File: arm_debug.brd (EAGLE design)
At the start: 40.3 x 19 mm, 11 parts

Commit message: Saving place.. currently working on Rev B
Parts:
- removed DEBUG: (no value), pinhead:1X06
- removed LED2: (no value), led:SML0805
- removed TP_5V, TP_GND0, TP_GND1, TP_VCC: 1625854-3, 1625854-3:RESC1608X50N
- added C1, C2: (no value), resistor:C0805
- added IC1: FT230XSS, FT230XS:SSOP16
- added JP1, JP2, PWR_SELECT: (no value), pinhead:1X03
- added P1: 0473460001, 0473460001:MOLEX_0473460001
- added R2, R3, R4, R6, R7: (no value), resistor:R0805
- added TP1, TP2, TP4: TPTP20SQ, testpad:TP20SQ
- added U1: CAT6219, CAT6219-330TDGT3:SOT-23(OT)5_LEAD
- moved LED1 16.1 mm to (29.2, 23.5), turned to 270 degrees
- moved R1 13.5 mm to (40.6, 17.1)
- moved DEVICE 8.98 mm to (21.6, 21.6)
- moved PROG 8.98 mm to (8.89, 21.6)
- moved R5 6.84 mm to (29.2, 19.1)
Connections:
- removed net !CTS: DEBUG.2
- removed net !RTS: DEBUG.6
- removed net VCC: DEVICE.1, PROG.1, R1.2, TP_VCC.1, TP_VCC.2
- new net +3V3: PWR_SELECT.3, TP2.TP, U1.5
- new net D+: C2.1, IC1.8, R7.1
- new net D-: C1.1, IC1.9, R1.1
- new net FT230_RX: IC1.4, JP1.2
- new net FT230_TX: IC1.1, JP2.2
- new net N$3: IC1.10, IC1.11, IC1.3
- new net N$4: P1.3, R7.2
- new net N$7: JP2.3, R4.1, R6.2
- new net N$8: JP1.3, R2.2, R3.1
- new net TARGET_PWR: DEVICE.1, PROG.1, PWR_SELECT.2
- net +5V: now also IC1.12, P1.1, PWR_SELECT.1, TP1.TP, U1.1, U1.3; no longer DEBUG.3, TP_5V.1, TP_5V.2
- net DEBUG_UART_RX: now also JP2.1, R4.2; no longer DEBUG.4
- net DEBUG_UART_TX: now also JP1.1, R3.2; no longer DEBUG.5
- net GND: now also C1.2, C2.2, IC1.13, IC1.5, P1.5, R2.1, R6.1, TP4.TP, U1.2; no longer DEBUG.1, LED2.C, TP_GND0.1, TP_GND0.2, TP_GND1.1, TP_GND1.2
- net N$2: now also P1.2, R1.2; no longer LED2.A, R1.1
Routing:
- net TARGET_PWR: track 0.00 -> 76.4 mm, vias 0 -> 2
- net +5V: track 43.8 -> 97.9 mm, vias 0 -> 3
- net +3V3: track 0.00 -> 44.3 mm
- net VCC: track 43.0 -> 0.00 mm
- net D+: track 0.00 -> 21.3 mm
- net FT230_TX: track 0.00 -> 20.5 mm
- net DEBUG_UART_TX: track 19.5 -> 38.9 mm, vias 2 -> 1
- net D-: track 0.00 -> 15.7 mm
- net FT230_RX: track 0.00 -> 12.3 mm
- net GND: track 32.0 -> 41.4 mm, vias 5 -> 1
- net N$3: track 0.00 -> 7.14 mm
- net N$8: track 0.00 -> 6.75 mm
- net N$7: track 0.00 -> 6.75 mm
- net N$4: track 0.00 -> 4.98 mm
- net DEBUG_UART_RX: track 27.6 -> 31.6 mm, vias 2 -> 1
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- added copper zone on layer 1, net GND
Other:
- board size 40.3 x 19 mm -> 50.5 x 27.9 mm
- board text added: "+3.3V"
- board text added: "+5V"
- board text added: "GND"
- board text added: "Power Select"
- board text added: "Rev B"
- board text added: "TARGET"
- board text added: "UART Level Shift"
- board text removed: "Rev A"

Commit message: Committing RevB
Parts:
- removed IC1: FT230XSS, FT230XS:SSOP16
- removed JP1, JP2, PWR_SELECT: (no value), pinhead:1X03
- removed R6: (no value), resistor:R0805
- removed TP1, TP2, TP4: TPTP20SQ, testpad:TP20SQ
- added C3: .1uF, resistor:C0603
- added LED2, LED3: (no value), led:CHIPLED_0603
- added S1: 431151015826, 431151015826:431181015816
- C1, C2: value (none) -> 47pF; device resistor:C0805 -> resistor:C0603
- LED1: device led:SML0805 -> led:CHIPLED_0603
- R1, R4, R7: value (none) -> 27; device resistor:R0805 -> resistor:R0603
- R2, R3: value (none) -> 330; device resistor:R0805 -> resistor:R0603
- R5: value (none) -> 1K; device resistor:R0805 -> resistor:R0603
- U1: value CAT6219 -> FT230XQ-T; device CAT6219-330TDGT3:SOT-23(OT)5_LEAD -> FT230XQ-T:QFN16
- moved R4 17.2 mm to (41.9, 8.57), turned to 180 degrees
- moved R2 16.6 mm to (41.9, 19.7), turned to 180 degrees
- moved LED1 16.3 mm to (45.1, 19.7)
- moved R3 15.9 mm to (41.9, 21.9), turned to 180 degrees
- moved R5 15.6 mm to (16.8, 9.53), turned to 180 degrees
- moved C1 14.0 mm to (41.9, 10.8), turned to 0 degrees
- moved U1 10.5 mm to (35.6, 14.0), turned to 180 degrees
- moved P1 10.2 mm to (45.4, 14.0), turned to 90 degrees
- moved DEVICE 9.16 mm to (26.7, 14.0)
- moved PROG 8.03 mm to (6.35, 14.0)
- moved C2 5.62 mm to (41.9, 17.5), turned to 0 degrees
- moved R1 4.32 mm to (41.9, 13.0), turned to 0 degrees
- moved R7 4.26 mm to (41.9, 15.2), turned to 0 degrees
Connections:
- removed net +3V3: PWR_SELECT.3, TP2.TP, U1.5
- removed net FT230_RX: IC1.4, JP1.2
- removed net FT230_TX: IC1.1, JP2.2
- removed net N$1: LED1.A, R5.1
- removed net N$7: JP2.3, R4.1, R6.2
- removed net N$8: JP1.3, R2.2, R3.1
- new net N$14: LED1.A, R2.1
- new net N$9: LED2.A, R3.1
- new net RXLED: LED2.C, U1.5
- new net TXLED: LED1.C, U1.11
- new net VCCIO: C3.1, R2.2, R3.2, U1.1, U1.8, U1.9
- net !RESET: now also R5.1, S1.2
- net +5V: now also R4.2, U1.10; no longer IC1.12, PWR_SELECT.1, R5.2, TP1.TP, U1.1, U1.3
- net D+: now also U1.6; no longer IC1.8
- net D-: now also U1.7; no longer IC1.9
- net DEBUG_UART_RX: now also U1.15; no longer JP2.1, R4.2
- net DEBUG_UART_TX: now also U1.2; no longer JP1.1, R3.2
- net GND: now also C3.2, LED3.C, S1.1, S1.GND1, S1.GND2, U1.13, U1.17, U1.3; no longer IC1.13, IC1.5, LED1.C, R2.1, R6.1, TP4.TP, U1.2
- net N$3: now also LED3.A, R4.1; no longer IC1.10, IC1.11, IC1.3
- net TARGET_PWR: now also R5.2; no longer PWR_SELECT.2
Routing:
- net +5V: track 97.9 -> 22.9 mm, vias 3 -> 0
- net TARGET_PWR: track 76.4 -> 24.4 mm, vias 2 -> 0
- net +3V3: track 44.3 -> 0.00 mm
- net GND: track 41.4 -> 4.54 mm, vias 1 -> 4
- net VCCIO: track 0.00 -> 23.7 mm, vias 0 -> 2
- net TXLED: track 0.00 -> 21.3 mm, vias 0 -> 2
- net FT230_TX: track 20.5 -> 0.00 mm
- net DEBUG_UART_TX: track 38.9 -> 20.4 mm, vias 1 -> 2
- net RXLED: track 0.00 -> 17.2 mm
- net D+: track 21.3 -> 8.51 mm
- net SWDCLK: track 16.9 -> 29.6 mm
- net !RESET: track 15.1 -> 27.6 mm
- net FT230_RX: track 12.3 -> 0.00 mm
- net SWDIO: track 15.2 -> 27.1 mm, vias 0 -> 2
- net DEBUG_UART_RX: track 31.6 -> 20.9 mm, vias 1 -> 2
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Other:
- board text added: "ARM Debug"
- board text added: "PWR"
- board text added: "RESET"
- board text added: "RX"
- board text added: "TX"
- board text removed: "+3.3V"
- board text removed: "+5V"
- board text removed: "ARM debug"
- board text removed: "GND"
- board text removed: "Power Select"
- board text removed: "TARGET"
- board text removed: "UART Level Shift"

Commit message: Commiting RevC
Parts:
- removed DEVICE, PROG: FTSH-105-01-L-DV-K, FTSH-105-01-L-DV-K:SAMTEC_FTSH-105-01-L-DV-K
- added P2: CORTEX-SWD, programming_headers:SAMTEC_FTSH-105-01-L-DV-K
- added P3: MOLEX_MICRO_USB, board_connectivity:047346-0001
- P1: value 0473460001 -> CORTEX-SWD; device 0473460001:MOLEX_0473460001 -> programming_headers:SAMTEC_FTSH-105-01-L-DV-K
- R4: value 27 -> 330
- S1: value 431151015826 -> WURTH_SMD_PB; device 431151015826:431181015816 -> switches:431181015816
- U1: value FT230XQ-T -> FT230X; device FT230XQ-T:QFN16 -> USB:QFN16
- moved P1 37.8 mm to (7.62, 14.0), turned to 0 degrees
- moved C3 1.93 mm to (33.7, 18.4)
- moved U1 1.27 mm to (34.3, 14.0)
- moved R5 0.32 mm to (16.5, 9.53)
- moved S1 0.32 mm to (16.5, 14.0)
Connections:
- removed net N/C: PROG.6, PROG.8
- net !RESET: now also P1.10, P2.10; no longer DEVICE.10, PROG.10
- net +5V: now also P3.1; no longer P1.1
- net DEBUG_UART_RX: now also P2.7; no longer DEVICE.6
- net DEBUG_UART_TX: now also P2.9; no longer DEVICE.8
- net GND: now also P1.3, P1.7, P1.9, P2.3, P2.5, P3.5, P3.P1, P3.P2, P3.P3, P3.P4, P3.P5, P3.P6; no longer DEVICE.3, DEVICE.5, DEVICE.7, DEVICE.9, PROG.3, PROG.5, PROG.7, PROG.9
- net N$2: now also P3.2; no longer P1.2
- net N$4: now also P3.3; no longer P1.3
- net RXLED: now also U1.11; no longer U1.5
- net SWDCLK: now also P1.4, P2.4; no longer DEVICE.4, PROG.4
- net SWDIO: now also P1.2, P2.2; no longer DEVICE.2, PROG.2
- net TARGET_PWR: now also P1.1, P2.1; no longer DEVICE.1, PROG.1
- net TXLED: now also U1.12; no longer U1.11
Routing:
- net TXLED: track 21.3 -> 29.8 mm, vias 2 -> 0
- net SWDCLK: track 29.6 -> 21.6 mm
- net RXLED: track 17.2 -> 24.7 mm
- net DEBUG_UART_RX: track 20.9 -> 14.1 mm, vias 2 -> 0
- net SWDIO: track 27.1 -> 20.7 mm
- net DEBUG_UART_TX: track 20.4 -> 15.4 mm, vias 2 -> 0
- net D-: track 11.3 -> 13.9 mm
- net GND: track 4.54 -> 2.13 mm, vias 4 -> 2
- net !RESET: track 27.6 -> 25.6 mm
- net +5V: track 22.9 -> 20.9 mm, vias 0 -> 2
- net D+: track 8.51 -> 9.98 mm
- net N/C: track 1.27 -> 0.00 mm
- net VCCIO: track 23.7 -> 22.6 mm
- net TARGET_PWR: track 24.4 -> 23.7 mm
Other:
- board text added: "PROG"
- board text added: "Rev C"
- board text added: "TARGET"
- board text removed: "Rev B"

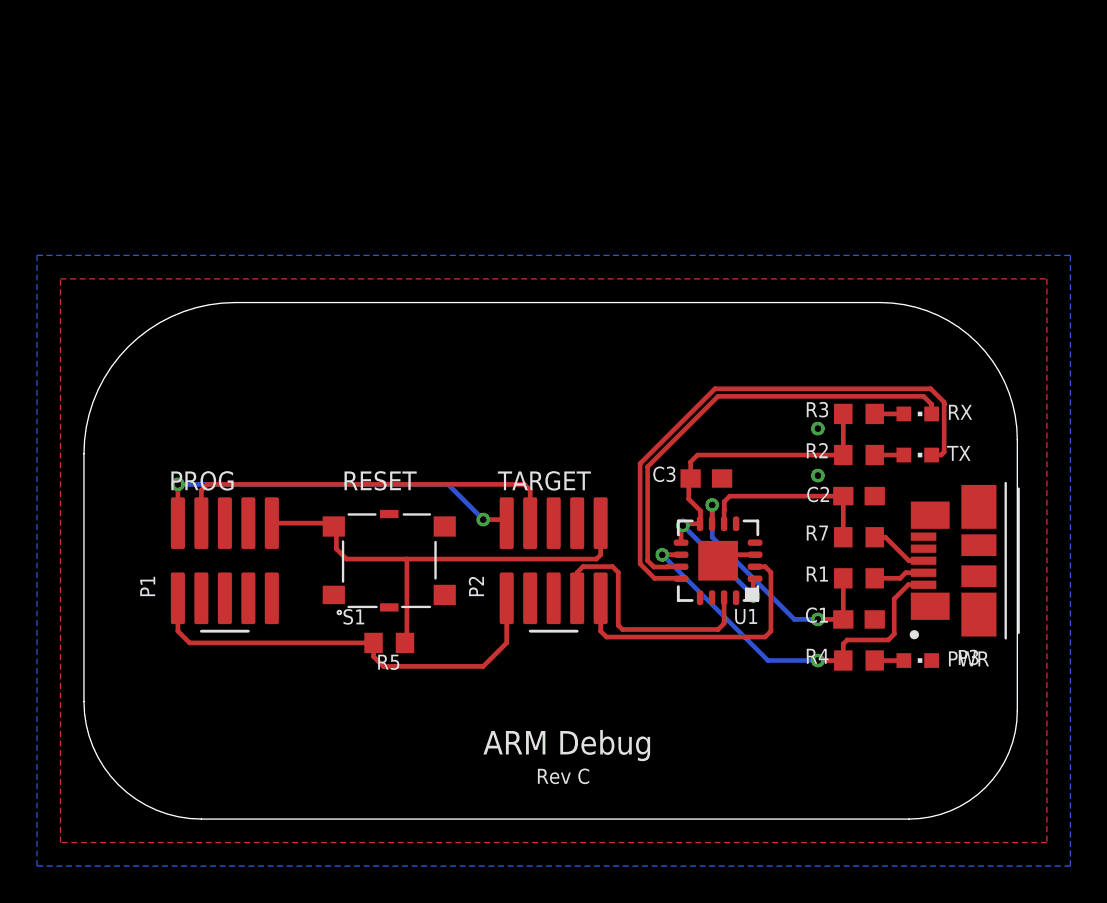
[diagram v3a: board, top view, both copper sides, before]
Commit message: Adding MEC connector for edge card connectors
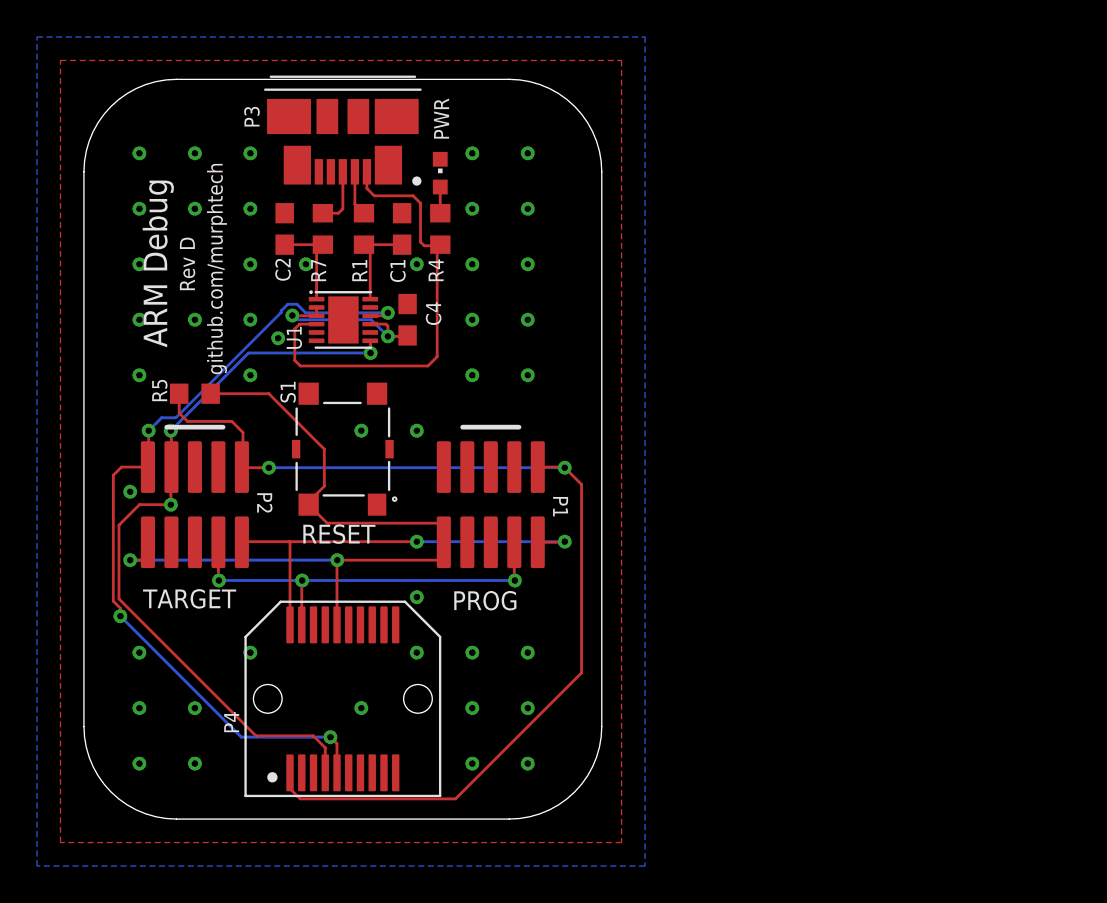
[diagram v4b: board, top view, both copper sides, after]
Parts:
- removed C3: .1uF, resistor:C0603
- removed LED1, LED2: (no value), led:CHIPLED_0603
- removed R2, R3: 330, resistor:R0603
- added C4: .1uF, resistor:C0603
- added P4: MEC6-110-02-L-D-RA1, programming_headers:MEC6-110-02-X-D-RAX-F
- P1, P2: value CORTEX-SWD -> FTSH-105-01-L-DV-K-TR
- U1: value FT230X -> FT234XD-T; device USB:QFN16 -> USB:DFN-12
- moved P3 37.8 mm to (14.0, 35.0), turned to 180 degrees
- moved LED3 36.9 mm to (19.3, 34.9), turned to 0 degrees
- moved C2 34.3 mm to (10.9, 31.9), turned to 90 degrees
- moved R7 33.4 mm to (12.9, 31.9), turned to 90 degrees
- moved R1 32.8 mm to (15.1, 31.9), turned to 90 degrees
- moved R4 32.5 mm to (19.3, 31.9), turned to 270 degrees
- moved C1 32.5 mm to (17.2, 31.9), turned to 90 degrees
- moved U1 24.1 mm to (14.0, 27.0), turned to 0 degrees
- moved P2 19.6 mm to (6.00, 17.0), turned to 180 degrees
- moved R5 17.1 mm to (6.00, 23.0)
- moved P1 14.7 mm to (22.0, 17.0), turned to 180 degrees
- moved S1 6.53 mm to (14.0, 20.0), turned to 90 degrees
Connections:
- removed net N$14: LED1.A, R2.1
- removed net N$9: LED2.A, R3.1
- removed net RXLED: LED2.C, U1.11
- removed net TXLED: LED1.C, U1.12
- removed net VCCIO: C3.1, R2.2, R3.2, U1.1, U1.8, U1.9
- new net !RESET#: C4.1, U1.2, U1.3, U1.9
- net !RESET: now also P4.10
- net +5V: now also U1.4; no longer U1.10
- net D+: now also U1.1; no longer U1.6
- net D-: now also U1.12; no longer U1.7
- net DEBUG_UART_RX: now also P4.7, U1.7; no longer U1.15
- net DEBUG_UART_TX: now also P4.9, U1.10; no longer U1.2
- net GND: now also C4.2, P4.3, P4.5, U1.5; no longer C3.2, U1.17, U1.3
- net SWDCLK: now also P4.4
- net SWDIO: now also P4.2
- net TARGET_PWR: now also P4.1
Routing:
- net TARGET_PWR: track 23.7 -> 56.9 mm, vias 0 -> 2
- net TXLED: track 29.8 -> 0.00 mm
- net DEBUG_UART_TX: track 15.4 -> 45.0 mm, vias 0 -> 4
- net DEBUG_UART_RX: track 14.1 -> 40.4 mm, vias 0 -> 3
- net RXLED: track 24.7 -> 0.00 mm
- net VCCIO: track 22.6 -> 0.00 mm, vias 2 -> 0
- net !RESET: track 25.6 -> 42.7 mm, vias 0 -> 2
- net !RESET#: track 0.00 -> 10.0 mm, vias 0 -> 2
- net D-: track 13.9 -> 5.08 mm, vias 2 -> 0
- net D+: track 9.98 -> 5.10 mm
- net +5V: track 20.9 -> 24.5 mm, vias 2 -> 0
- net SWDIO: track 20.7 -> 23.5 mm
- net GND: track 2.13 -> 0.00 mm, vias 2 -> 44
- net N$9: track 1.58 -> 0.00 mm
- net N$14: track 1.58 -> 0.00 mm
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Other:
- board size 50.5 x 27.9 mm -> 28 x 40 mm
- board text added: "Rev D"
- board text added: "github.com/murphtech"
- board text removed: "RX"
- board text removed: "Rev C"
- board text removed: "TX"
